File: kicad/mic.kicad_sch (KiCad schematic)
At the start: 3 parts

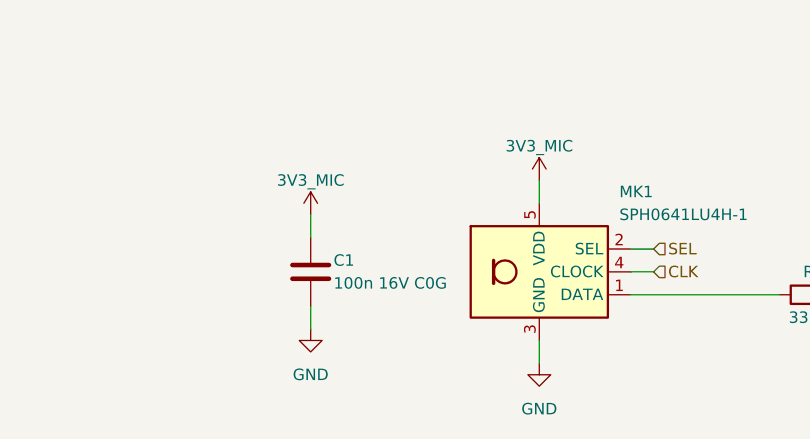
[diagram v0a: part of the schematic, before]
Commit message: Block-diagram top page, power review fixes, readable sheets
Top level
- Page 1 is now a block diagram of the signal flow (FPGA -> headers ->
  clock buffers / TX drive -> transceivers -> ADCs -> FPGA, mics, power).
- New group sheets hold the reused cells: tx (16 tx_group + 4 en_buf),
  array (64 channel), adcs (8 adc), mics (8 mic), clocks (7 clk_buf).
  Power and headers stay directly under the top. All written by gen_top.py,
  which now also survives a kicad-cli re-save of a cell sheet.

Power (review findings)
- Polyfuse 1812L200/16DR (16 V), TPS65131RGER stated explicitly, input caps
  2 x 10u 1206, 50 V caps on 12 V, inductor values carry minimum Isat.
- +3V3: TLV75733P (ceramic-stable) replaces TLV1117-33.
- New JP5/JP6 isolate +-6V5; every rail: REG node -> jumper -> rail with TP,
  LED (not on analog LDOs) and PWR_FLAG.
- Power sheet is now generated by build_cells.py in a 2x3 block layout
  (build_power.py removed).

Readability and small fixes
- Rails on sideways pins use labelled flags; sideways GND symbols hide text.
- tx_group: 595 outputs wired straight to the drivers.
- Title blocks on every sheet; channel sheet notes and field placement fixed
  (sch_fields.py --only, sch_annotate.py).
- ADC_SDI 10k pull-down, ADC reset/DOUT notes, mic cap 50 V.
- ERC 0 violations, 1,704 parts. PDFs: docs/schematics/00..13.
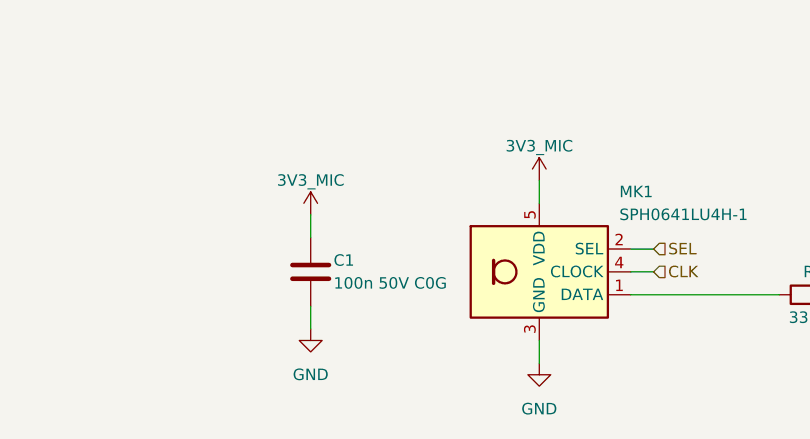
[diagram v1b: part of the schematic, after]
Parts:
- C1: value 100n 16V C0G -> 100n 50V C0G
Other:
- company: (none) -> Hybrid 8x8 ultrasonic AESA
- title: (none) -> MEMS mic (x8): SPH0641LU4H-1

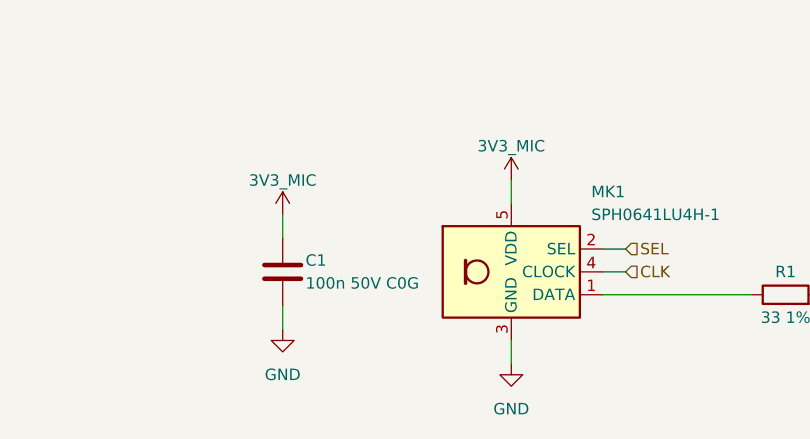
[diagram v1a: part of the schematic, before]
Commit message: Optimized, costed BOM with LCSC numbers for every part
scripts/bom.py picks parts (Basic first, stock margin) and writes docs/bom.md,
fab/bom_jlcpcb.csv and scripts/parts.json; sch_lcsc.py fills LCSC fields from it.
Part changes: TPS7A4700RGWT for the out-of-stock TPS7A4701, BAV99 C2500, SS54 in SMA,
SMD1812P200TF16 polyfuse, 600R ferrite, Basic-value +5V/VDRV dividers (VDRV 15.4 V),
Sunlord SWPA6045 footprints, mic 100 nF C0G in 1206. AD7606C-16 and SPH0641 now
assembled by JLCPCB.
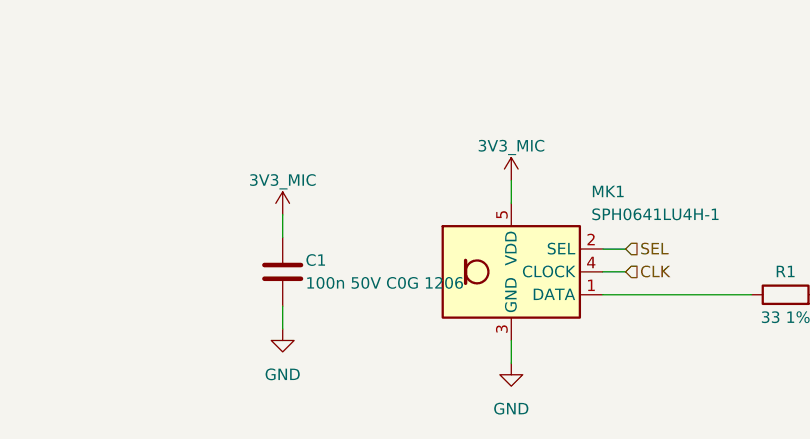
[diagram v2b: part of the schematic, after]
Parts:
- C1: value 100n 50V C0G -> 100n 50V C0G 1206; footprint Capacitor_SMD:C_0805_2012Metric -> Capacitor_SMD:C_1206_3216Metric; LCSC TBD -> C170182
- MK1: LCSC consigned -> C2879853
- R1: LCSC TBD -> C23140
